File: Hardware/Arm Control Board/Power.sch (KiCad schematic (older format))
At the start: 65 parts

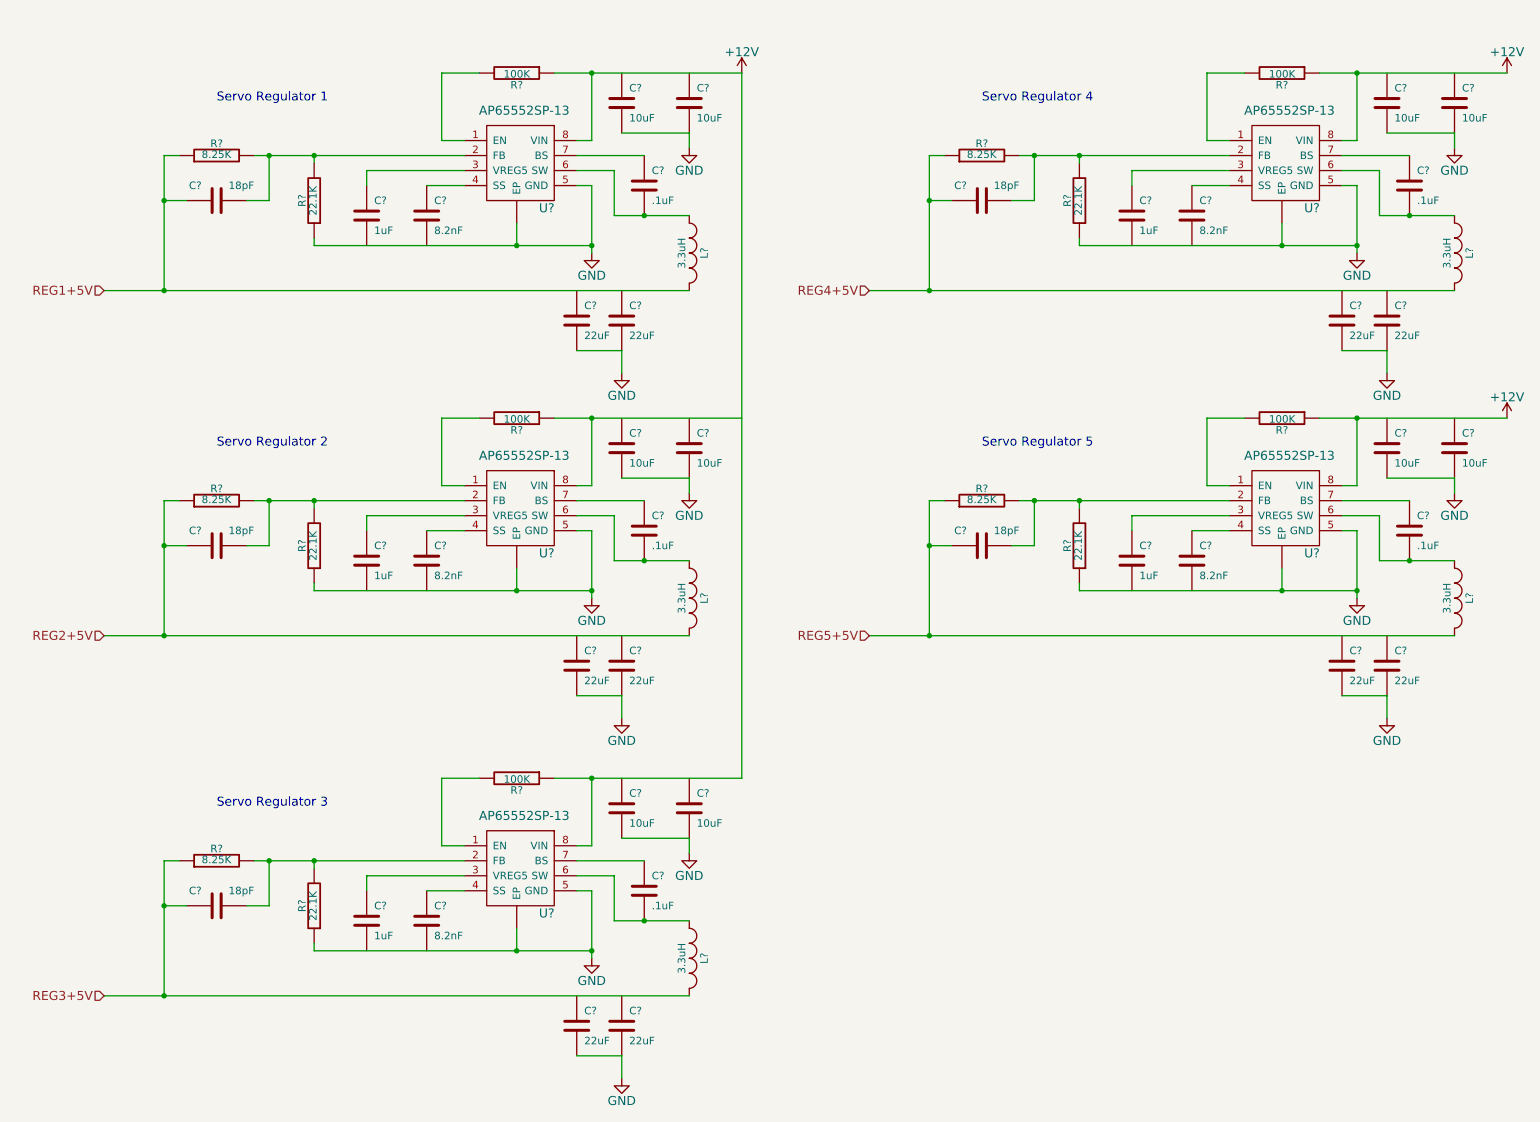
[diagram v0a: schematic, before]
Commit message: Added enable pins to all servo regulators
Might not need them all independent, we'll see
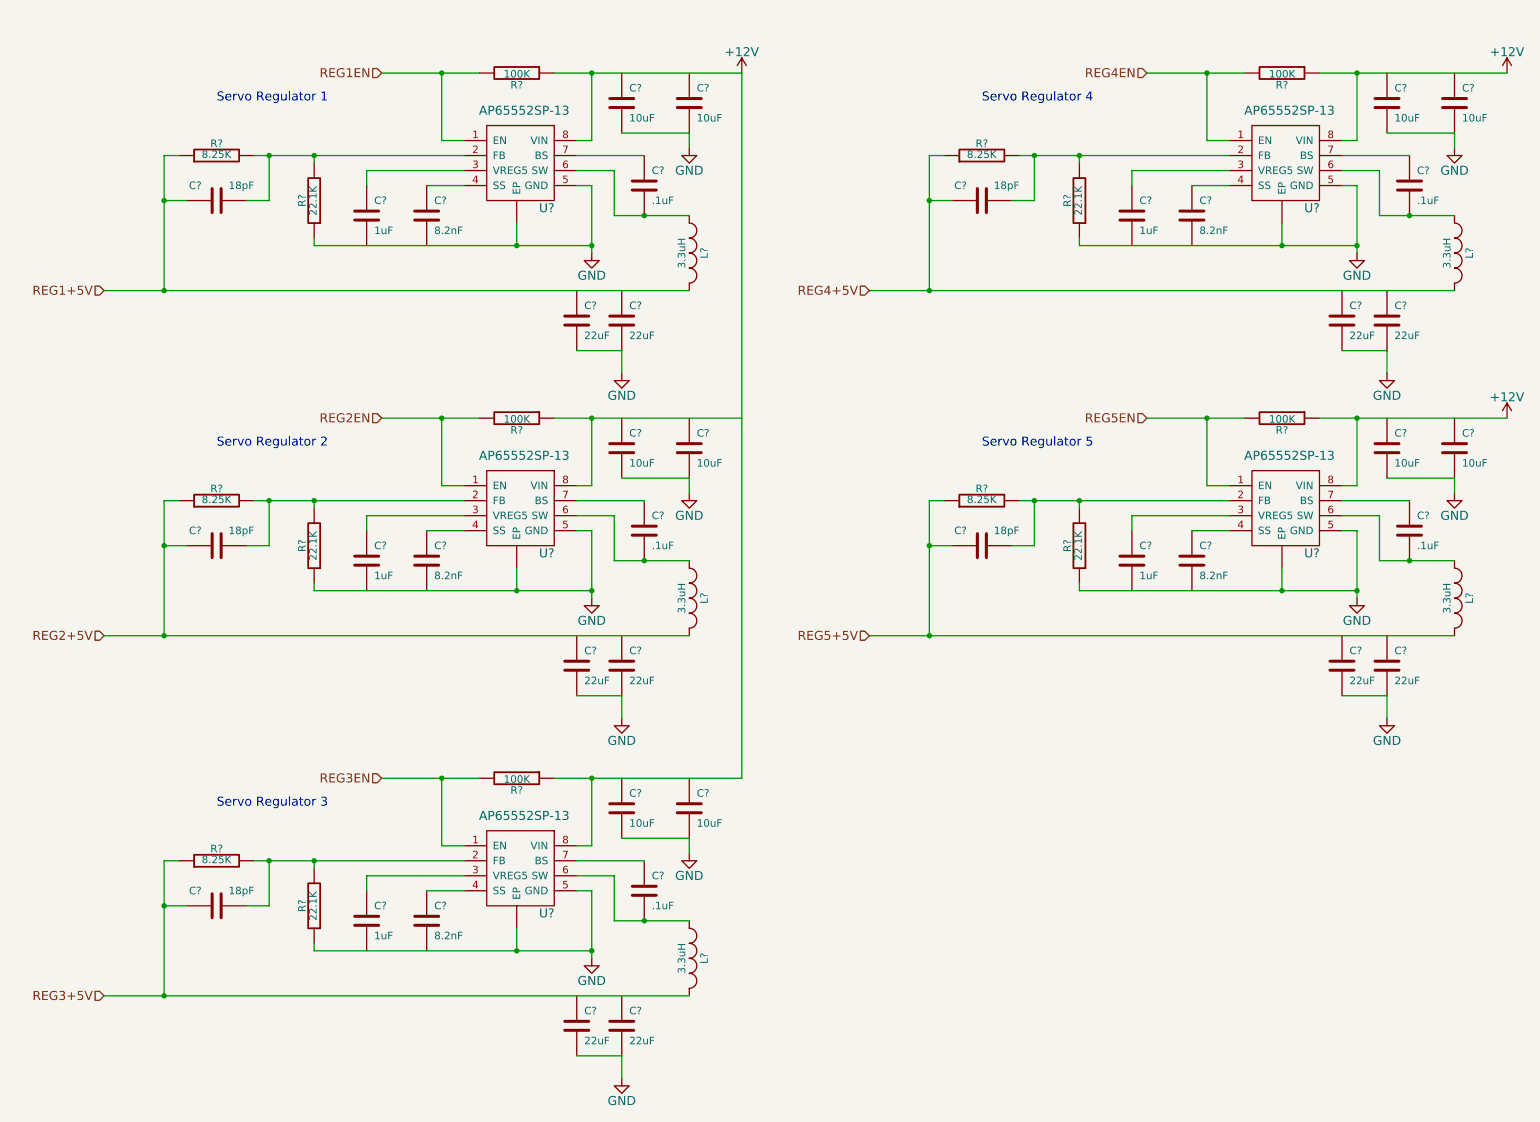
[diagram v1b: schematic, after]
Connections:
- net REG1EN: now reaches R?.2, U?.1 (EN)
- net REG2EN: now reaches R?.2, U?.1 (EN)
- net REG3EN: now reaches R?.2, U?.1 (EN)
- net REG4EN: now reaches R?.2, U?.1 (EN)
- net REG5EN: now reaches R?.2, U?.1 (EN)
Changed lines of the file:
@@
 $EndComp
 Wire Wire Line
-	3750 750  3500 750
+	3100 750  3750 750
 Wire Wire Line
 	3500 750  3500 1200
@@
 	3500 1200 3650 1200
 Wire Wire Line
-	4250 750  4500 750
-Wire Wire Line
-	4500 750  5500 750
+	4250 750  5500 750
 Wire Wire Line
 	4500 750  4500 1200
@@
 $EndComp
 Wire Wire Line
-	1250 2200 1650 2200
-Wire Wire Line
-	1650 2200 5150 2200
+	1250 2200 5150 2200
 $Comp
 L C C?
@@
 	4400 1500 4500 1500
 Wire Wire Line
-	4500 1500 4500 1900
-Wire Wire Line
-	4500 1900 4500 1950
+	4500 1500 4500 1950
 $Comp
 L C C?
@@
 $EndComp
 Wire Wire Line
-	2250 1300 2350 1300
-Wire Wire Line
-	2350 1300 2650 1300
-Wire Wire Line
-	2650 1300 3650 1300
+	2250 1300 3650 1300
 Wire Wire Line
 	2650 1300 2650 1350
 Wire Wire Line
-	2650 1900 4000 1900
-Wire Wire Line
-	4000 1900 4500 1900
+	2650 1900 4500 1900
 Connection ~ 4500 1900
 Wire Wire Line
@@
 	1800 1600 1650 1600
 Wire Wire Line
-	1650 1300 1650 1600
-Wire Wire Line
-	1650 1600 1650 2200
+	1650 1300 1650 2200
 Wire Wire Line
 	1650 1300 1750 1300
@@
 	4650 1400 4650 1700
 Wire Wire Line
-	4650 1700 4850 1700
-Wire Wire Line
-	4850 1700 5150 1700
+	4650 1700 5150 1700
 Connection ~ 4850 1700
 Text Notes 2000 950  0    60   ~ 0
@@
 $EndComp
 Wire Wire Line
-	3750 3050 3500 3050
+	3100 3050 3750 3050
 Wire Wire Line
 	3500 3050 3500 3500
@@
 	3500 3500 3650 3500
 Wire Wire Line
-	4250 3050 4500 3050
-Wire Wire Line
-	4500 3050 5500 3050
+	4250 3050 5500 3050
 Wire Wire Line
 	4500 3050 4500 3500
@@
 $EndComp
 Wire Wire Line
-	1250 4500 1650 4500
-Wire Wire Line
-	1650 4500 5150 4500
+	1250 4500 5150 4500
 $Comp
 L C C?
@@
 	4400 3800 4500 3800
 Wire Wire Line
-	4500 3800 4500 4200
-Wire Wire Line
-	4500 4200 4500 4250
+	4500 3800 4500 4250
 $Comp
 L C C?
@@
 $EndComp
 Wire Wire Line
-	2250 3600 2350 3600
-Wire Wire Line
-	2350 3600 2650 3600
-Wire Wire Line
-	2650 3600 3650 3600
+	2250 3600 3650 3600
 Wire Wire Line
 	2650 3600 2650 3650
 Wire Wire Line
-	2650 4200 4000 4200
-Wire Wire Line
-	4000 4200 4500 4200
+	2650 4200 4500 4200
 Connection ~ 4500 4200
 Wire Wire Line
@@
 	1800 3900 1650 3900
 Wire Wire Line
-	1650 3600 1650 3900
-Wire Wire Line
-	1650 3900 1650 4500
+	1650 3600 1650 4500
 Wire Wire Line
 	1650 3600 1750 3600
@@
 	4650 3700 4650 4000
 Wire Wire Line
-	4650 4000 4850 4000
-Wire Wire Line
-	4850 4000 5150 4000
+	4650 4000 5150 4000
 Connection ~ 4850 4000
 Text Notes 2000 3250 0    60   ~ 0
@@
 $EndComp
 Wire Wire Line
-	3750 5450 3500 5450
+	3100 5450 3750 5450
 Wire Wire Line
 	3500 5450 3500 5900
@@
 	3500 5900 3650 5900
 Wire Wire Line
-	4250 5450 4500 5450
-Wire Wire Line
-	4500 5450 5500 5450
+	4250 5450 5500 5450
 Wire Wire Line
 	4500 5450 4500 5900
@@
 $EndComp
 Wire Wire Line
-	1250 6900 1650 6900
-Wire Wire Line
-	1650 6900 5150 6900
+	1250 6900 5150 6900
 $Comp
 L C C?
@@
 	4400 6200 4500 6200
 Wire Wire Line
-	4500 6200 4500 6600
-Wire Wire Line
-	4500 6600 4500 6650
+	4500 6200 4500 6650
 $Comp
 L C C?
@@
 $EndComp
 Wire Wire Line
-	2250 6000 2350 6000
-Wire Wire Line
-	2350 6000 2650 6000
-Wire Wire Line
-	2650 6000 3650 6000
+	2250 6000 3650 6000
 Wire Wire Line
 	2650 6000 2650 6050
 Wire Wire Line
-	2650 6600 4000 6600
-Wire Wire Line
-	4000 6600 4500 6600
+	2650 6600 4500 6600
 Connection ~ 4500 6600
 Wire Wire Line
@@
 	1800 6300 1650 6300
 Wire Wire Line
-	1650 6000 1650 6300
-Wire Wire Line
-	1650 6300 1650 6900
+	1650 6000 1650 6900
 Wire Wire Line
 	1650 6000 1750 6000
@@
 	4650 6100 4650 6400
 Wire Wire Line
-	4650 6400 4850 6400
-Wire Wire Line
-	4850 6400 5150 6400
+	4650 6400 5150 6400
 Connection ~ 4850 6400
 Text Notes 2000 5650 0    60   ~ 0
@@
 $EndComp
 Wire Wire Line
-	8850 750  8600 750
+	8200 750  8850 750
 Wire Wire Line
 	8600 750  8600 1200
@@
 	8600 1200 8750 1200
 Wire Wire Line
-	9350 750  9600 750
-Wire Wire Line
-	9600 750  10600 750
+	9350 750  10600 750
 Wire Wire Line
 	9600 750  9600 1200
@@
 $EndComp
 Wire Wire Line
-	6350 2200 6750 2200
-Wire Wire Line
-	6750 2200 10250 2200
+	6350 2200 10250 2200
 $Comp
 L C C?
@@
 	9500 1500 9600 1500
 Wire Wire Line
-	9600 1500 9600 1900
-Wire Wire Line
-	9600 1900 9600 1950
+	9600 1500 9600 1950
 $Comp
 L C C?
@@
 $EndComp
 Wire Wire Line
-	7350 1300 7450 1300
-Wire Wire Line
-	7450 1300 7750 1300
-Wire Wire Line
-	7750 1300 8750 1300
+	7350 1300 8750 1300
 Wire Wire Line
 	7750 1300 7750 1350
 Wire Wire Line
-	7750 1900 9100 1900
-Wire Wire Line
-	9100 1900 9600 1900
+	7750 1900 9600 1900
 Connection ~ 9600 1900
 Wire Wire Line
@@
 	6900 1600 6750 1600
 Wire Wire Line
-	6750 1300 6750 1600
-Wire Wire Line
-	6750 1600 6750 2200
+	6750 1300 6750 2200
 Wire Wire Line
 	6750 1300 6850 1300
@@
 	9750 1400 9750 1700
 Wire Wire Line
-	9750 1700 9950 1700
-Wire Wire Line
-	9950 1700 10250 1700
+	9750 1700 10250 1700
 Connection ~ 9950 1700
 Text Notes 7100 950  0    60   ~ 0
@@
 $EndComp
 Wire Wire Line
-	8850 3050 8600 3050
+	8200 3050 8850 3050
 Wire Wire Line
 	8600 3050 8600 3500
@@
 	8600 3500 8750 3500
 Wire Wire Line
-	9350 3050 9600 3050
-Wire Wire Line
-	9600 3050 10600 3050
+	9350 3050 10600 3050
 Wire Wire Line
 	9600 3050 9600 3500
@@
 $EndComp
 Wire Wire Line
-	6350 4500 6750 4500
-Wire Wire Line
-	6750 4500 10250 4500
+	6350 4500 10250 4500
 $Comp
 L C C?
@@
 	9500 3800 9600 3800
 Wire Wire Line
-	9600 3800 9600 4200
-Wire Wire Line
-	9600 4200 9600 4250
+	9600 3800 9600 4250
 $Comp
 L C C?
@@
 $EndComp
 Wire Wire Line
-	7350 3600 7450 3600
-Wire Wire Line
-	7450 3600 7750 3600
-Wire Wire Line
-	7750 3600 8750 3600
+	7350 3600 8750 3600
 Wire Wire Line
 	7750 3600 7750 3650
 Wire Wire Line
-	7750 4200 9100 4200
-Wire Wire Line
-	9100 4200 9600 4200
+	7750 4200 9600 4200
 Connection ~ 9600 4200
 Wire Wire Line
@@
 	6900 3900 6750 3900
 Wire Wire Line
-	6750 3600 6750 3900
-Wire Wire Line
-	6750 3900 6750 4500
+	6750 3600 6750 4500
 Wire Wire Line
 	6750 3600 6850 3600
@@
 	9750 3700 9750 4000
 Wire Wire Line
-	9750 4000 9950 4000
-Wire Wire Line
-	9950 4000 10250 4000
+	9750 4000 10250 4000
 Connection ~ 9950 4000
 Text Notes 7100 3250 0    60   ~ 0
@@
 	1    0    0    -1
 $EndComp
+Connection ~ 8600 3050
+Text HLabel 8200 3050 0    60   Input ~ 0
+REG5EN
+Text HLabel 8200 750  0    60   Input ~ 0
+REG4EN
+Connection ~ 8600 750
+Text HLabel 3100 5450 0    60   Input ~ 0
+REG3EN
+Connection ~ 3500 5450
+Text HLabel 3100 3050 0    60   Input ~ 0
+REG2EN
+Connection ~ 3500 3050
+Text HLabel 3100 750  0    60   Input ~ 0
+REG1EN
+Connection ~ 3500 750
 $EndSCHEMATC

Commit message: Added and connected servo plugs
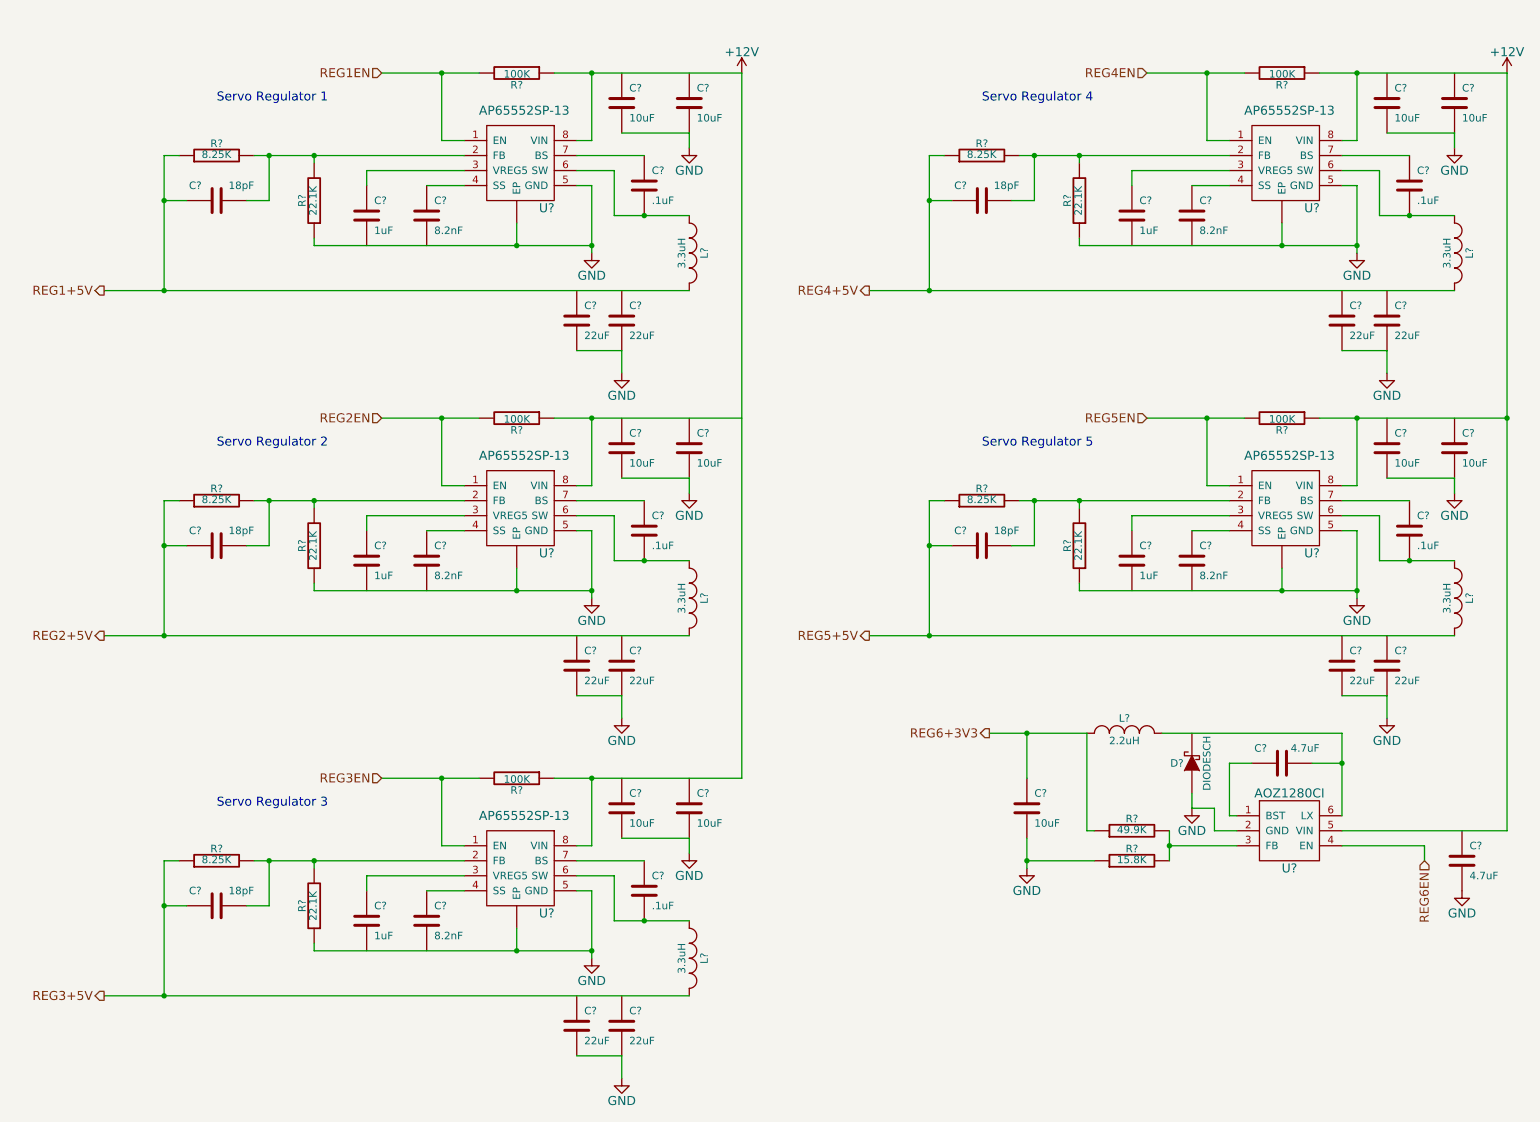
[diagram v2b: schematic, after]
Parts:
- added C? (x2): 4.7uF, symbol C
- added C?: 10uF, symbol C
- added D?: DIODESCH, symbol DIODESCH
- added L?: 2.2uH, symbol INDUCTOR_SMALL
- added R?: 15.8K, symbol R
- added R?: 49.9K, symbol R
- added U?: AOZ1280CI, symbol AOZ1280CI
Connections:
- net +12V: now also U?.5 (VIN)
- net GND: now also C?.2, C?.2, D?.1 (A), R?.1, U?.2 (GND)
- new net: C?.1, U?.1 (BST)
- new net: R?.2, R?.2, U?.3 (FB)
- new net: C?.2, L?.2, U?.6 (LX)
- new net REG6+3V3: C?.1, L?.1, R?.1
- new net REG6EN: U?.4 (EN)
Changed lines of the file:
@@
 Text Notes 2000 950  0    60   ~ 0
 Servo Regulator 1
-Text HLabel 1250 2200 0    60   Input ~ 0
+Text HLabel 1250 2200 0    60   Output ~ 0
 REG1+5V
 $Comp
@@
 Text Notes 2000 3250 0    60   ~ 0
 Servo Regulator 2
-Text HLabel 1250 4500 0    60   Input ~ 0
+Text HLabel 1250 4500 0    60   Output ~ 0
 REG2+5V
 $Comp
@@
 Text Notes 2000 5650 0    60   ~ 0
 Servo Regulator 3
-Text HLabel 1250 6900 0    60   Input ~ 0
+Text HLabel 1250 6900 0    60   Output ~ 0
 REG3+5V
 $Comp
@@
 Text Notes 7100 950  0    60   ~ 0
 Servo Regulator 4
-Text HLabel 6350 2200 0    60   Input ~ 0
+Text HLabel 6350 2200 0    60   Output ~ 0
 REG4+5V
 $Comp
@@
 Text Notes 7100 3250 0    60   ~ 0
 Servo Regulator 5
-Text HLabel 6350 4500 0    60   Input ~ 0
+Text HLabel 6350 4500 0    60   Output ~ 0
 REG5+5V
-$Comp
-L +12V #PWR?
-U 1 1 54C6E3E4
-P 10600 3050
-F 0 "#PWR?" H 10600 2900 60  0001 C CNN
-F 1 "+12V" H 10600 3190 60  0000 C CNN
-F 2 "" H 10600 3050 60  0000 C CNN
-F 3 "" H 10600 3050 60  0000 C CNN
-	1    10600 3050
-	1    0    0    -1
-$EndComp
 Connection ~ 8600 3050
 Text HLabel 8200 3050 0    60   Input ~ 0
@@
 REG1EN
 Connection ~ 3500 750
+$Comp
+L AOZ1280CI U?
+U 1 1 54C78E4A
+P 9350 5700
+F 0 "U?" H 9150 5350 60  0000 C CNN
+F 1 "AOZ1280CI" H 9150 5850 60  0000 C CNN
+F 2 "" H 9350 5700 60  0000 C CNN
+F 3 "" H 9350 5700 60  0000 C CNN
+	1    9350 5700
+	1    0    0    -1
+$EndComp
+Wire Wire Line
+	10600 5800 9500 5800
+$Comp
+L C C?
+U 1 1 54C7A7D0
+P 10300 6000
+F 0 "C?" H 10350 6100 50  0000 L CNN
+F 1 "4.7uF" H 10350 5900 50  0000 L CNN
+F 2 "" H 10338 5850 30  0000 C CNN
+F 3 "" H 10300 6000 60  0000 C CNN
+	1    10300 6000
+	1    0    0    -1
+$EndComp
+$Comp
+L GND #PWR?
+U 1 1 54C7A8A9
+P 10300 6200
+F 0 "#PWR?" H 10300 5950 60  0001 C CNN
+F 1 "GND" H 10300 6050 60  0000 C CNN
+F 2 "" H 10300 6200 60  0000 C CNN
+F 3 "" H 10300 6200 60  0000 C CNN
+	1    10300 6200
+	1    0    0    -1
+$EndComp
+Wire Wire Line
+	9500 5900 10050 5900
+Wire Wire Line
+	10050 5900 10050 6000
+Text HLabel 10050 6000 3    60   Input ~ 0
+REG6EN
+Wire Wire Line
+	10600 750  10600 5800
+Connection ~ 10600 3050
+$Comp
+L INDUCTOR_SMALL L?
+U 1 1 54C7DB1A
+P 8050 5150
+F 0 "L?" H 8050 5250 50  0000 C CNN
+F 1 "2.2uH" H 8050 5100 50  0000 C CNN
+F 2 "" H 8050 5150 60  0000 C CNN
+F 3 "" H 8050 5150 60  0000 C CNN
+	1    8050 5150
+	1    0    0    -1
+$EndComp
+Wire Wire Line
+	9500 5700 9500 5150
+Wire Wire Line
+	9500 5150 8300 5150
+$Comp
+L R R?
+U 1 1 54C7EE9A
+P 8100 6000
+F 0 "R?" V 8180 6000 50  0000 C CNN
+F 1 "15.8K" V 8107 6001 50  0000 C CNN
+F 2 "" V 8030 6000 30  0000 C CNN
+F 3 "" H 8100 6000 30  0000 C CNN
+	1    8100 6000
+	0    -1   -1   0
+$EndComp
+$Comp
+L R R?
+U 1 1 54C7F0B3
+P 8100 5800
+F 0 "R?" V 8180 5800 50  0000 C CNN
+F 1 "49.9K" V 8107 5801 50  0000 C CNN
+F 2 "" V 8030 5800 30  0000 C CNN
+F 3 "" H 8100 5800 30  0000 C CNN
+	1    8100 5800
+	0    -1   -1   0
+$EndComp
+Wire Wire Line
+	8800 5900 8350 5900
+Wire Wire Line
+	8350 5800 8350 6000
+Connection ~ 8350 5900
+Wire Wire Line
+	7800 5150 7800 5800
+Wire Wire Line
+	7800 5800 7850 5800
+$Comp
+L DIODESCH D?
+U 1 1 54C7FCA6
+P 8500 5350
+F 0 "D?" V 8500 5450 50  0000 C CNN
+F 1 "DIODESCH" H 8500 5250 50  0000 C CNN
+F 2 "" H 8500 5350 60  0000 C CNN
+F 3 "" H 8500 5350 60  0000 C CNN
+	1    8500 5350
+	0    -1   -1   0
+$EndComp
+$Comp
+L GND #PWR?
+U 1 1 54C809C1
+P 7400 6050
+F 0 "#PWR?" H 7400 5800 60  0001 C CNN
+F 1 "GND" H 7400 5900 60  0000 C CNN
+F 2 "" H 7400 6050 60  0000 C CNN
+F 3 "" H 7400 6050 60  0000 C CNN
+	1    7400 6050
+	1    0    0    -1
+$EndComp
+Wire Wire Line
+	7150 5150 7800 5150
+$Comp
+L C C?
+U 1 1 54C81C2A
+P 7400 5650
+F 0 "C?" H 7450 5750 50  0000 L CNN
+F 1 "10uF" H 7450 5550 50  0000 L CNN
+F 2 "" H 7438 5500 30  0000 C CNN
+F 3 "" H 7400 5650 60  0000 C CNN
+	1    7400 5650
+	1    0    0    -1
+$EndComp
+Wire Wire Line
+	7400 5450 7400 5150
+Connection ~ 7400 5150
+Wire Wire Line
+	8800 5800 8650 5800
+Wire Wire Line
+	8650 5800 8650 5650
+Wire Wire Line
+	8650 5650 8500 5650
+Wire Wire Line
+	8500 5650 8500 5550
+$Comp
+L GND #PWR?
+U 1 1 54C83114
+P 8500 5650
+F 0 "#PWR?" H 8500 5400 60  0001 C CNN
+F 1 "GND" H 8500 5500 60  0000 C CNN
+F 2 "" H 8500 5650 60  0000 C CNN
+F 3 "" H 8500 5650 60  0000 C CNN
+	1    8500 5650
+	1    0    0    -1
+$EndComp
+Wire Wire Line
+	7400 5850 7400 6050
+Wire Wire Line
+	7400 6000 7850 6000
+Connection ~ 7400 6000
+$Comp
+L C C?
+U 1 1 54C846DE
+P 9100 5350
+F 0 "C?" V 9200 5450 50  0000 L CNN
+F 1 "4.7uF" V 9200 5100 50  0000 L CNN
+F 2 "" H 9138 5200 30  0000 C CNN
+F 3 "" H 9100 5350 60  0000 C CNN
+	1    9100 5350
+	0    -1   -1   0
+$EndComp
+Wire Wire Line
+	8900 5350 8750 5350
+Wire Wire Line
+	8750 5350 8750 5700
+Wire Wire Line
+	8750 5700 8800 5700
+Wire Wire Line
+	9300 5350 9500 5350
+Connection ~ 9500 5350
+Text HLabel 7150 5150 0    60   Output ~ 0
+REG6+3V3
 $EndSCHEMATC
